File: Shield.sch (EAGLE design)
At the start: 0 parts

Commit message: Added SD Card Circuit
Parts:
- added 0-7, 14-21, 21-37, 22-36, 38-52, 39-53, A0-A7, A8-A15, POWER: 8PINHEADERN, LEMS:8PINHEADERN
- added 0.1UF, 0.1UF-2: CERAMICCAPL, LEMS:CERAMICCAPL
- added 100UF, 100UF-2: ELECTROLYTICCAPS, LEMS:ELECTROLYTICCAPS
- added 10K, 1K, 1K_2, 2.2K, 2.2K-2, 2.2K-3, 2.2K-4: RESISTORT, LEMS:RESISTORT
- added 3.3VI2C, 5VI2CTERM: 2PINHEADERS, LEMS:2PINHEADERS
- added 5V, GND, LEDPINS, U$2: 2PINHEADERN, LEMS:2PINHEADERN
- added 8-13: 10PINHEADERN, LEMS:10PINHEADERN
- added BATT: (no value), LEMS:CR1220THM
- added DS1307: DS1307P, LEMS:DS1307P
- added LED1, LED2: (no value), LEMS:LED3MM
- added S1: (no value), LEMS:10-XXN
- added SDLVLS: 74AHC125N, LEMS:74AHC125N
- added U$1: SDMMC06132, LEMS:SDMMC06132
- added U$4, U$7: MOSFETNN, LEMS:MOSFETNN
- added U$9: MCP1700-330T, LEMS:MCP1700-330T
- added Y1: (no value), LEMS:CRYSTALTC38H
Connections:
- new net 3.3V: 0.1UF-2.1, 100UF-2.1, 2.2K-3.2, 2.2K-4.2, SDLVLS4.OE, SDLVLSPWRN.VCC, U$1.VDD, U$4.G, U$7.G, U$9.VOUT
- new net 3.3V_SCL: 2.2K-4.1, 3.3VI2C.1, U$7.S
- new net 3.3V_SDA: 2.2K-3.1, 3.3VI2C.2, U$4.S
- new net 5V: 0.1UF.1, 100UF.1, 10K.1, 2.2K-2.1, 2.2K.1, 5V.1, 5V.2, DS1307.VCC, U$9.VCC
- new net AREF: 8-13.3
- new net CRYSTAL: DS1307.X1, Y1.2
- new net GND: 0.1UF-2.2, 0.1UF.2, 100UF-2.2, 100UF.2, 8-13.4, BATT.-, DS1307.GND, LED1.C, LED2.C, S1.P, S1.P1, SDLVLS1.OE, SDLVLS2.OE, SDLVLS3.OE, SDLVLSPWRN.GND, U$1.COMMON_SW, U$1.GND, U$1.VSS1, U$1.VSS2, U$9.GND
- new net GREENLED: 1K_2.2, LEDPINS.2
- new net MISO_SOFT: 8-13.6, U$1.DATA_OUT
- new net MOSI_SOFT: 8-13.7, SDLVLS2.A
- new net N$1: 8-13.1
- new net N$10: 8-13.10
- new net N$11: 0-7.1
- new net N$12: 0-7.2
- new net N$13: 0-7.3
- new net N$14: 0-7.4
- new net N$15: 0-7.5
- new net N$16: 0-7.6
- new net N$17: 0-7.7
- new net N$18: 0-7.8
- new net N$19: 14-21.1
- new net N$2: 8-13.2
- new net N$20: 14-21.2
- new net N$21: 14-21.3
- new net N$22: 14-21.4
- new net N$23: 14-21.5
- new net N$24: 14-21.6
- new net N$27: 21-37.1
- new net N$28: 21-37.2
- new net N$29: 21-37.3
- new net N$30: 21-37.4
- new net N$31: 21-37.5
- new net N$32: 21-37.6
- new net N$33: 21-37.7
- new net N$34: 21-37.8
- new net N$35: 39-53.1
- new net N$36: 39-53.2
- new net N$37: 39-53.3
- new net N$38: 39-53.4
- new net N$39: 39-53.5
- new net N$40: 39-53.6
- new net N$41: 39-53.7
- new net N$42: 39-53.8
- new net N$43: 22-36.1
- new net N$44: 22-36.2
- new net N$45: 22-36.3
- new net N$46: 22-36.4
- new net N$47: 22-36.5
- new net N$48: 22-36.6
- new net N$49: 22-36.7
- new net N$50: 22-36.8
- new net N$51: 38-52.1
- new net N$52: 38-52.2
- new net N$53: 38-52.3
- new net N$54: 38-52.4
- new net N$55: 38-52.5
- new net N$56: 38-52.6
- new net N$57: 38-52.7
- new net N$58: 38-52.8
- new net N$59: A8-A15.8
- new net N$60: A8-A15.7
- new net N$61: A8-A15.6
- new net N$62: A8-A15.5
- new net N$63: A8-A15.4
- new net N$64: A8-A15.3
- new net N$65: A8-A15.2
- new net N$66: A8-A15.1
- new net N$67: A0-A7.8
- new net N$68: A0-A7.7
- new net N$69: A0-A7.6
- new net N$70: A0-A7.5
- new net N$71: A0-A7.4
- new net N$72: A0-A7.3
- new net N$73: A0-A7.2
- new net N$74: A0-A7.1
- new net N$75: POWER.8
- new net N$76: POWER.7
- new net N$77: POWER.6
- new net N$78: POWER.5
- new net N$79: POWER.4
- new net N$81: POWER.2
- new net N$82: POWER.1
- new net N$83: 1K.1, LED1.A
- new net N$84: 1K_2.1, LED2.A
- new net N$86: DS1307.X2, Y1.1
- new net N$87: BATT.+, BATT.+1, DS1307.VBAT
- new net N$9: 8-13.9
- new net REDLED: 1K.2, LEDPINS.1
- new net RESET: POWER.3, S1.S, S1.S1
- new net SCK_SOFT: 8-13.5, SDLVLS1.A
- new net SCL: 14-21.8, 2.2K.2, 5VI2CTERM.1, DS1307.SCL, U$7.D
- new net SDA: 14-21.7, 2.2K-2.2, 5VI2CTERM.2, DS1307.SDA, U$4.D
- new net SD_CD: U$1.CARD_DETECT, U$2.1
- new net SD_CSIN: SDLVLS3.Y, U$1.CS
- new net SD_DATAIN: SDLVLS2.Y, U$1.DATA_IN
- new net SD_SCKIN: SDLVLS1.Y, U$1.SCLK
- new net SD_WP: U$1.WRITE_PROTECT, U$2.2
- new net SQW: DS1307.SQW
- new net SS_SOFT: 10K.2, 8-13.8, SDLVLS3.A
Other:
- note added: "1"

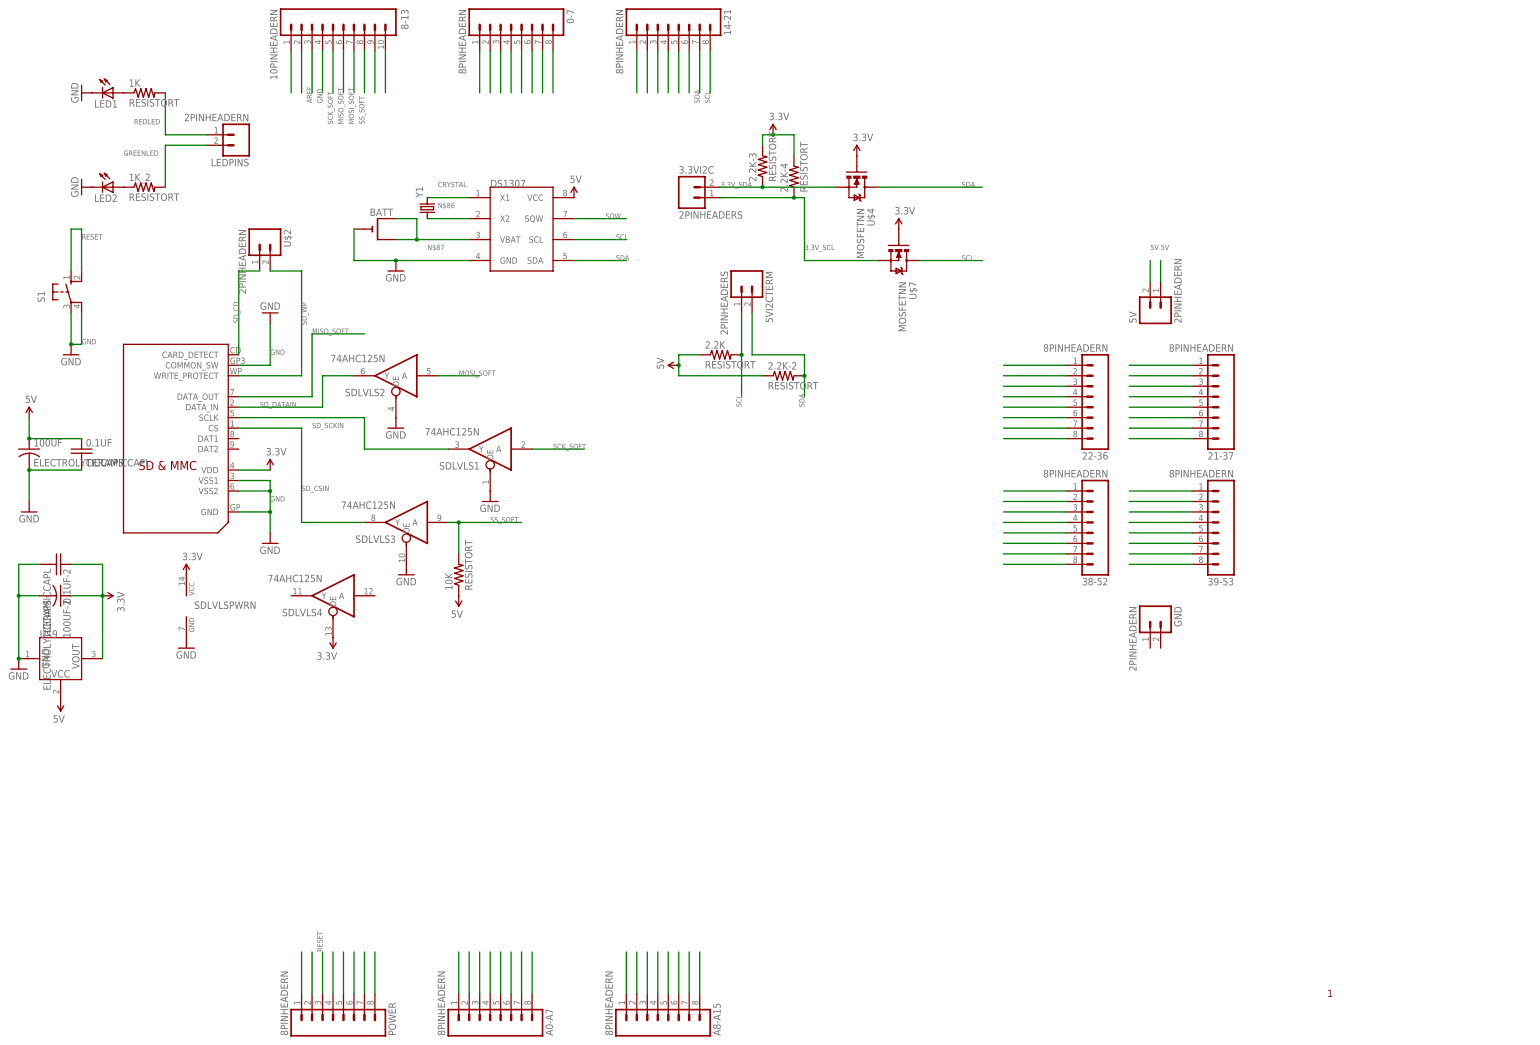
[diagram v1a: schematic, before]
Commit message: Added names and various details
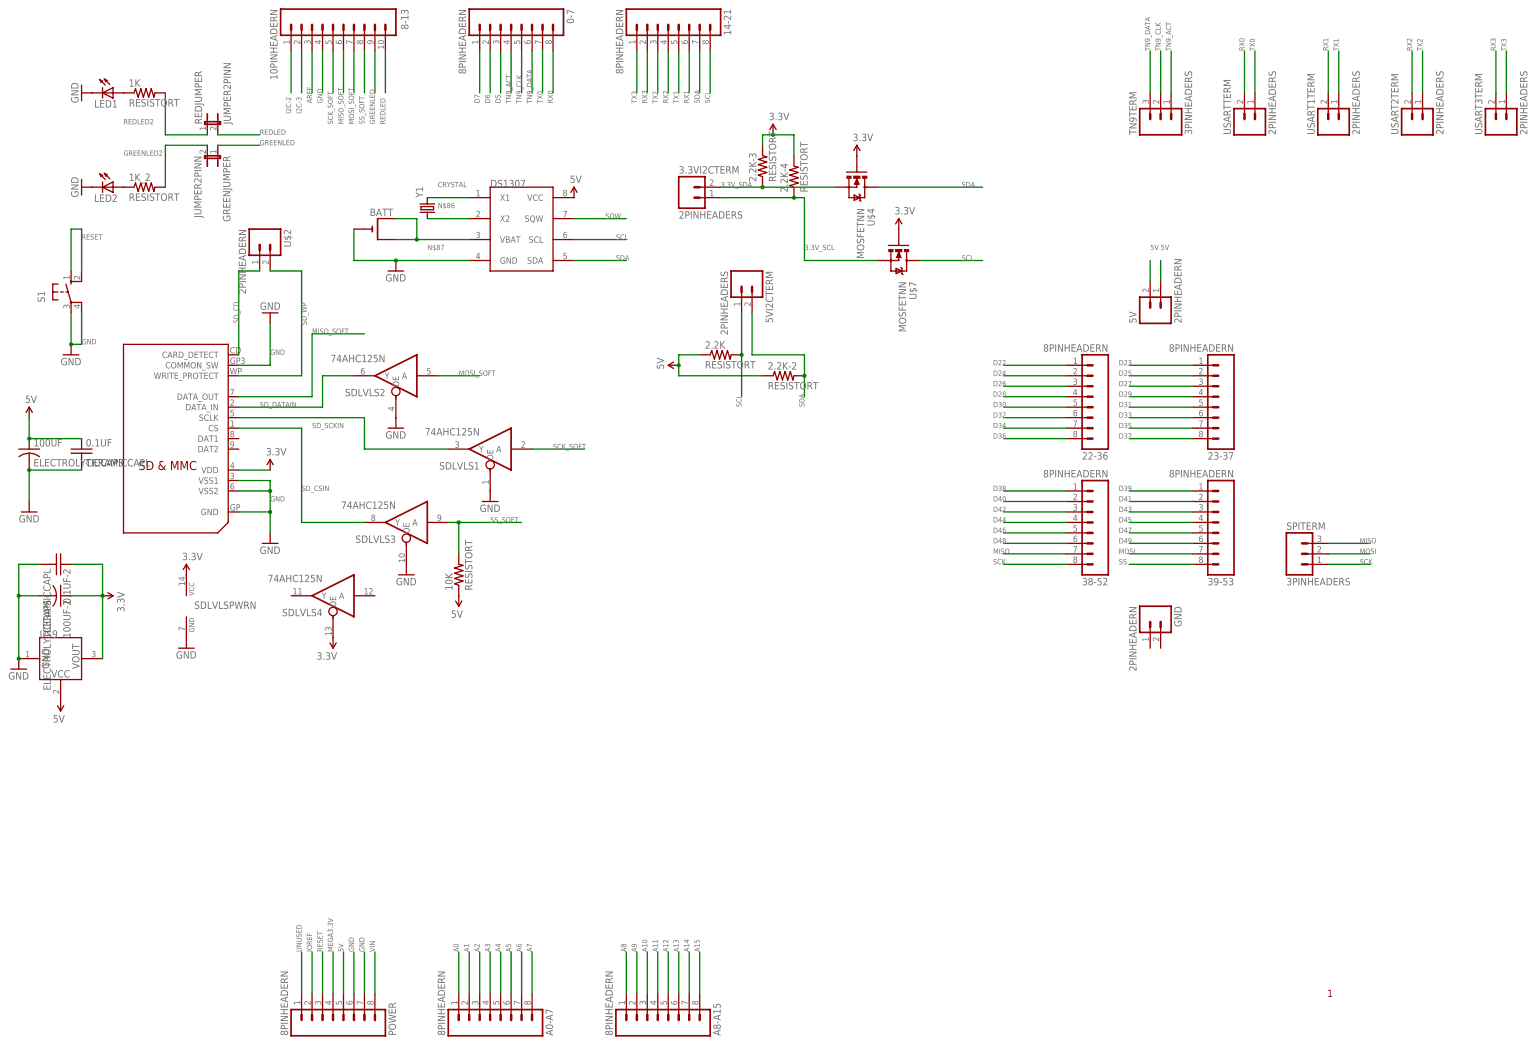
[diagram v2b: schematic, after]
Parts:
- removed LEDPINS: 2PINHEADERN, LEMS:2PINHEADERN
- added GREENJUMPER, REDJUMPER: JUMPER2PINN, LEMS:JUMPER2PINN
- added SPITERM, TN9TERM: 3PINHEADERS, LEMS:3PINHEADERS
- added USART1TERM, USART2TERM, USART3TERM, USARTTERM: 2PINHEADERS, LEMS:2PINHEADERS
- renumbered 21-37 to 23-37, 3.3VI2C to 3.3VI2CTERM
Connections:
- net N$1 renamed I2C-2
- net N$11 renamed D7
- net N$12 renamed D6
- net N$13 renamed D5
- net N$2 renamed I2C-3
- net N$27 renamed D23
- net N$28 renamed D25
- net N$29 renamed D27
- net N$30 renamed D29
- net N$31 renamed D31
- net N$32 renamed D33
- net N$33 renamed D35
- net N$34 renamed D37
- net N$35 renamed D39
- net N$36 renamed D41
- net N$37 renamed D43
- net N$38 renamed D45
- net N$39 renamed D47
- net N$40 renamed D49
- net N$42 renamed SS
- net N$43 renamed D22
- net N$44 renamed D24
- net N$45 renamed D26
- net N$46 renamed D28
- net N$47 renamed D30
- net N$48 renamed D32
- net N$49 renamed D34
- net N$50 renamed D36
- net N$51 renamed D38
- net N$52 renamed D40
- net N$53 renamed D42
- net N$54 renamed D44
- net N$55 renamed D46
- net N$56 renamed D48
- net N$59 renamed A15
- net N$60 renamed A14
- net N$61 renamed A13
- net N$62 renamed A12
- net N$63 renamed A11
- net N$64 renamed A10
- net N$65 renamed A9
- net N$66 renamed A8
- net N$67 renamed A7
- net N$68 renamed A6
- net N$69 renamed A5
- net N$70 renamed A4
- net N$71 renamed A3
- net N$72 renamed A2
- net N$73 renamed A1
- net N$74 renamed A0
- net N$75 renamed VIN
- net N$79 renamed MEGA3.3V
- net N$81 renamed IOREF
- net N$82 renamed UNUSED
- removed net N$10: 8-13.10
- removed net N$14: 0-7.4
- removed net N$15: 0-7.5
- removed net N$16: 0-7.6
- removed net N$17: 0-7.7
- removed net N$18: 0-7.8
- removed net N$19: 14-21.1
- removed net N$20: 14-21.2
- removed net N$21: 14-21.3
- removed net N$22: 14-21.4
- removed net N$23: 14-21.5
- removed net N$24: 14-21.6
- removed net N$41: 39-53.7
- removed net N$57: 38-52.7
- removed net N$58: 38-52.8
- removed net N$76: POWER.7
- removed net N$77: POWER.6
- removed net N$78: POWER.5
- removed net N$9: 8-13.9
- new net GREENLED2: 1K_2.2, GREENJUMPER.2
- new net MISO: 38-52.7, SPITERM.3
- new net MOSI: 39-53.7, SPITERM.2
- new net REDLED2: 1K.2, REDJUMPER.1
- new net RX0: 0-7.8, USARTTERM.2
- new net RX1: 14-21.6, USART1TERM.2
- new net RX2: 14-21.4, USART2TERM.2
- new net RX3: 14-21.2, USART3TERM.2
- new net SCK: 38-52.8, SPITERM.1
- new net TN9_ACT: 0-7.4, TN9TERM.1
- new net TN9_CLK: 0-7.5, TN9TERM.2
- new net TN9_DATA: 0-7.6, TN9TERM.3
- new net TX0: 0-7.7, USARTTERM.1
- new net TX1: 14-21.5, USART1TERM.1
- new net TX2: 14-21.3, USART2TERM.1
- new net TX3: 14-21.1, USART3TERM.1
- net 5V: now also POWER.5
- net GND: now also POWER.6, POWER.7
- net GREENLED: now also 8-13.9, GREENJUMPER.1; no longer 1K_2.2, LEDPINS.2
- net REDLED: now also 8-13.10, REDJUMPER.2; no longer 1K.2, LEDPINS.1

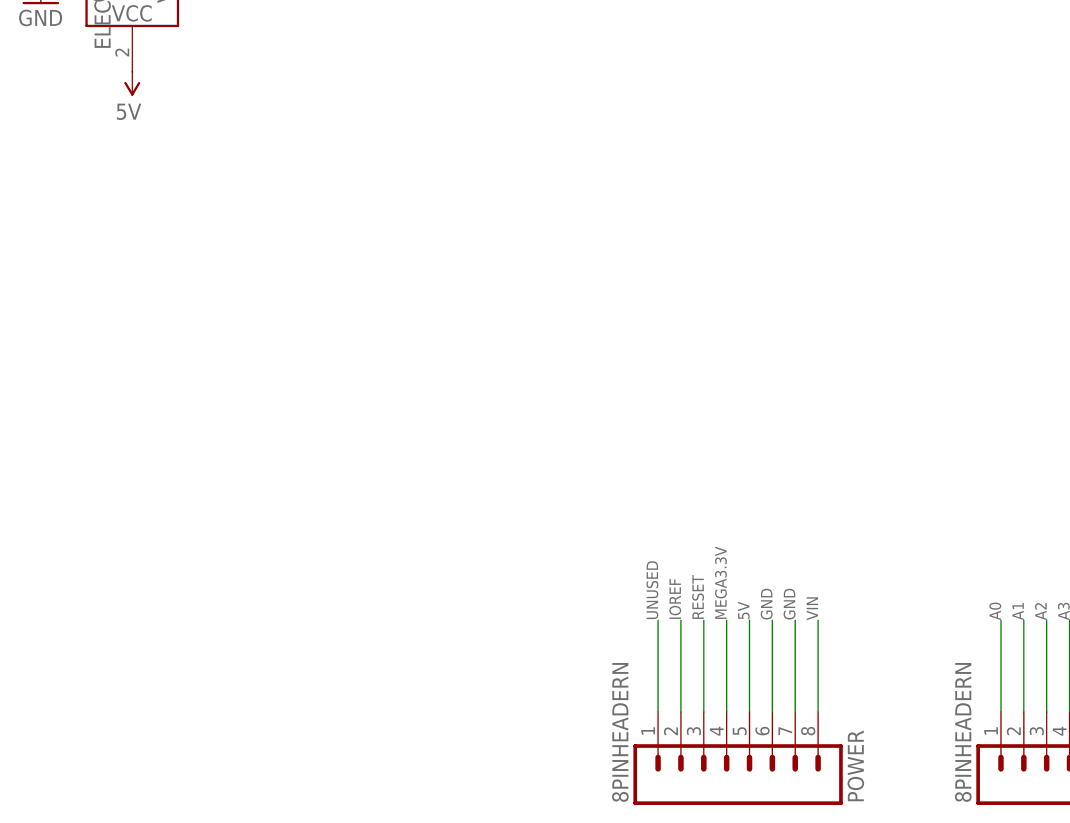
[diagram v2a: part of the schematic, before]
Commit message: Added 4.5V Reference
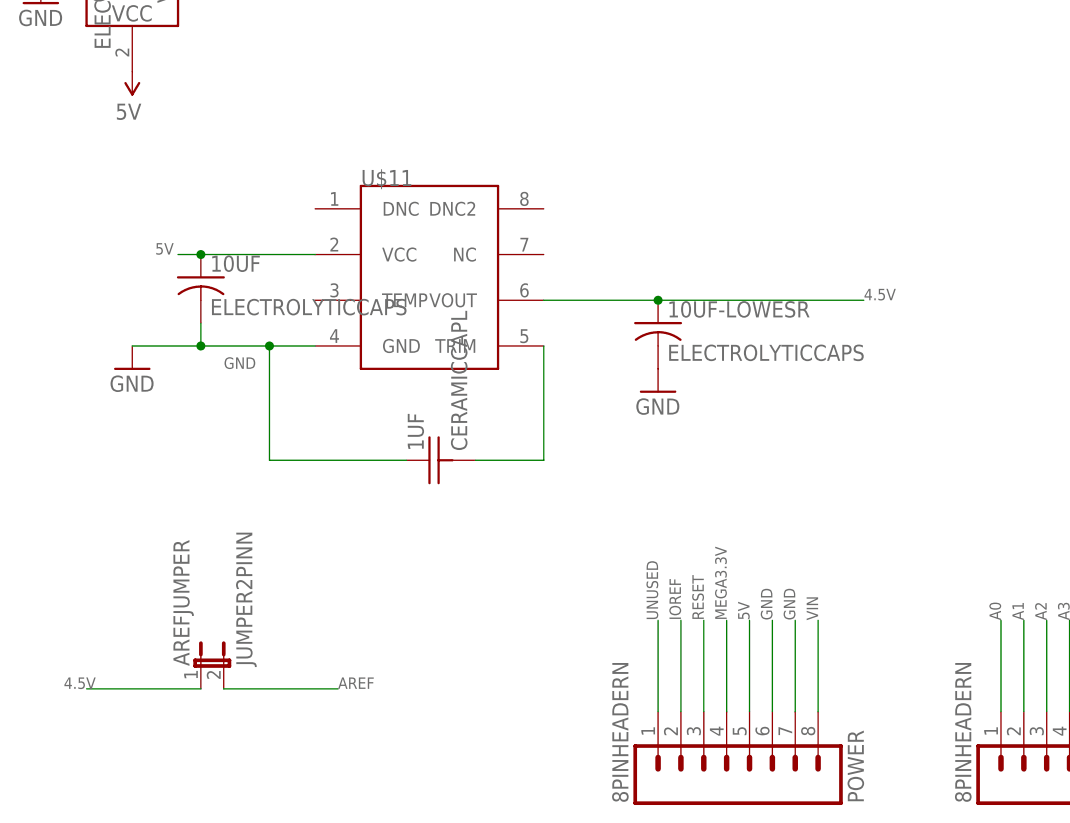
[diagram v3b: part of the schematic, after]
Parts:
- added 10UF, 10UF-LOWESR: ELECTROLYTICCAPS, LEMS:ELECTROLYTICCAPS
- added 1UF: CERAMICCAPL, LEMS:CERAMICCAPL
- added AREFJUMPER: JUMPER2PINN, LEMS:JUMPER2PINN
- added U$11: REF5045S, LEMS:REF5045S
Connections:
- new net 4.5V: 10UF-LOWESR.1, AREFJUMPER.1, U$11.VOUT
- new net N$1: 1UF.2, U$11.TRIM
- net 5V: now also 10UF.1, U$11.VCC
- net AREF: now also AREFJUMPER.2
- net GND: now also 10UF-LOWESR.2, 10UF.2, 1UF.1, U$11.GND
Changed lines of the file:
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@@
 <setting verticaltext="up"/>
 </settings>
-<grid distance="0.1" unitdist="inch" unit="inch" style="dots" multiple="1" display="yes" altdistance="0.01" altunitdist="inch" altunit="inch"/>
+<grid distance="0.1" unitdist="inch" unit="inch" style="lines" multiple="1" display="no" altdistance="0.01" altunitdist="inch" altunit="inch"/>
 <layers>
 <layer number="1" name="Top" color="4" fill="1" visible="no" active="no"/>
@@
 <part name="USART2TERM" library="LEMS" deviceset="2PINHEADER" device="S"/>
 <part name="USART3TERM" library="LEMS" deviceset="2PINHEADER" device="S"/>
+<part name="U$11" library="LEMS" deviceset="REF5045" device="S"/>
+<part name="1UF" library="LEMS" deviceset="CERAMICCAP" device="L"/>
+<part name="GND13" library="LEMS" deviceset="GND" device=""/>
+<part name="10UF" library="LEMS" deviceset="ELECTROLYTICCAP" device="S"/>
+<part name="10UF-LOWESR" library="LEMS" deviceset="ELECTROLYTICCAP" device="S"/>
+<part name="GND14" library="LEMS" deviceset="GND" device=""/>
+<part name="AREFJUMPER" library="LEMS" deviceset="JUMPER2PIN" device="N"/>
 </parts>
 <sheets>
@@
 <instance part="USART2TERM" gate="G$1" x="347.98" y="228.6" rot="R90"/>
 <instance part="USART3TERM" gate="G$1" x="368.3" y="228.6" rot="R90"/>
+<instance part="U$11" gate="REF5045" x="53.34" y="63.5"/>
+<instance part="1UF" gate="G$1" x="53.34" y="43.18" rot="R90"/>
+<instance part="GND13" gate="1" x="20.32" y="53.34"/>
+<instance part="10UF" gate="G$1" x="27.94" y="63.5"/>
+<instance part="10UF-LOWESR" gate="G$1" x="78.74" y="58.42"/>
+<instance part="GND14" gate="1" x="78.74" y="50.8"/>
+<instance part="AREFJUMPER" gate="G$1" x="27.94" y="20.32"/>
 </instances>
 <busses>
@@
 <label x="93.98" y="25.4" size="1.27" layer="95" rot="R90"/>
 </segment>
+<segment>
+<pinref part="U$11" gate="REF5045" pin="GND"/>
+<wire x1="40.64" y1="55.88" x2="35.56" y2="55.88" width="0.1524" layer="91"/>
+<pinref part="1UF" gate="G$1" pin="1"/>
+<wire x1="35.56" y1="55.88" x2="27.94" y2="55.88" width="0.1524" layer="91"/>
+<wire x1="27.94" y1="55.88" x2="20.32" y2="55.88" width="0.1524" layer="91"/>
+<wire x1="50.8" y1="43.18" x2="35.56" y2="43.18" width="0.1524" layer="91"/>
+<wire x1="35.56" y1="43.18" x2="35.56" y2="55.88" width="0.1524" layer="91"/>
+<junction x="35.56" y="55.88"/>
+<pinref part="GND13" gate="1" pin="GND"/>
+<pinref part="10UF" gate="G$1" pin="2"/>
+<wire x1="27.94" y1="58.42" x2="27.94" y2="55.88" width="0.1524" layer="91"/>
+<junction x="27.94" y="55.88"/>
+<label x="30.48" y="53.34" size="1.27" layer="95"/>
+</segment>
+<segment>
+<pinref part="10UF-LOWESR" gate="G$1" pin="2"/>
+<pinref part="GND14" gate="1" pin="GND"/>
+</segment>
 </net>
 <net name="MOSI_SOFT" class="0">
@@
 <label x="88.9" y="25.4" size="1.27" layer="95" rot="R90"/>
 </segment>
+<segment>
+<pinref part="U$11" gate="REF5045" pin="VCC"/>
+<wire x1="40.64" y1="66.04" x2="27.94" y2="66.04" width="0.1524" layer="91"/>
+<pinref part="10UF" gate="G$1" pin="1"/>
+<wire x1="27.94" y1="66.04" x2="25.4" y2="66.04" width="0.1524" layer="91"/>
+<junction x="27.94" y="66.04"/>
+<label x="22.86" y="66.04" size="1.27" layer="95"/>
+</segment>
 </net>
 <net name="I2C-2" class="0">
@@
 <wire x1="81.28" y1="243.84" x2="81.28" y2="233.68" width="0.1524" layer="91"/>
 <label x="81.28" y="231.14" size="1.27" layer="95" rot="R90"/>
+</segment>
+<segment>
+<pinref part="AREFJUMPER" gate="G$1" pin="2"/>
+<wire x1="30.48" y1="17.78" x2="43.18" y2="17.78" width="0.1524" layer="91"/>
+<label x="43.18" y="17.78" size="1.27" layer="95"/>
 </segment>
 </net>
@@
 </segment>
 </net>
+<net name="N$1" class="0">
+<segment>
+<pinref part="U$11" gate="REF5045" pin="TRIM"/>
+<wire x1="66.04" y1="55.88" x2="66.04" y2="43.18" width="0.1524" layer="91"/>
+<pinref part="1UF" gate="G$1" pin="2"/>
+<wire x1="66.04" y1="43.18" x2="58.42" y2="43.18" width="0.1524" layer="91"/>
+</segment>
+</net>
+<net name="4.5V" class="0">
+<segment>
+<pinref part="U$11" gate="REF5045" pin="VOUT"/>
+<pinref part="10UF-LOWESR" gate="G$1" pin="1"/>
+<wire x1="66.04" y1="60.96" x2="78.74" y2="60.96" width="0.1524" layer="91"/>
+<wire x1="78.74" y1="60.96" x2="101.6" y2="60.96" width="0.1524" layer="91"/>
+<junction x="78.74" y="60.96"/>
+<label x="101.6" y="60.96" size="1.27" layer="95"/>
+</segment>
+<segment>
+<pinref part="AREFJUMPER" gate="G$1" pin="1"/>
+<wire x1="15.24" y1="17.78" x2="27.94" y2="17.78" width="0.1524" layer="91"/>
+<label x="12.7" y="17.78" size="1.27" layer="95"/>
+</segment>
+</net>
